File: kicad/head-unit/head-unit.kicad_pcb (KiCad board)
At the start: 4 copper layers, 82 parts, among them J1 Debug_Port, J10 DAC+, J2 Relay_Main_Power, J3 Steering_Wheel, J4 Power_Port, J5 Remote, J6 Relay_Ign_Detect, J7 XT60-M, J8 I2C_Interface, J9 Pi, K1 Relay_Aux_Power, K2 Relay_Amplifier, Q1 NMOS, Q2 NMOS, SW1 SW_RST, U1 STM32F401RCTx, U2 TPS56339DDC, U3 ADP1108AN-3.3

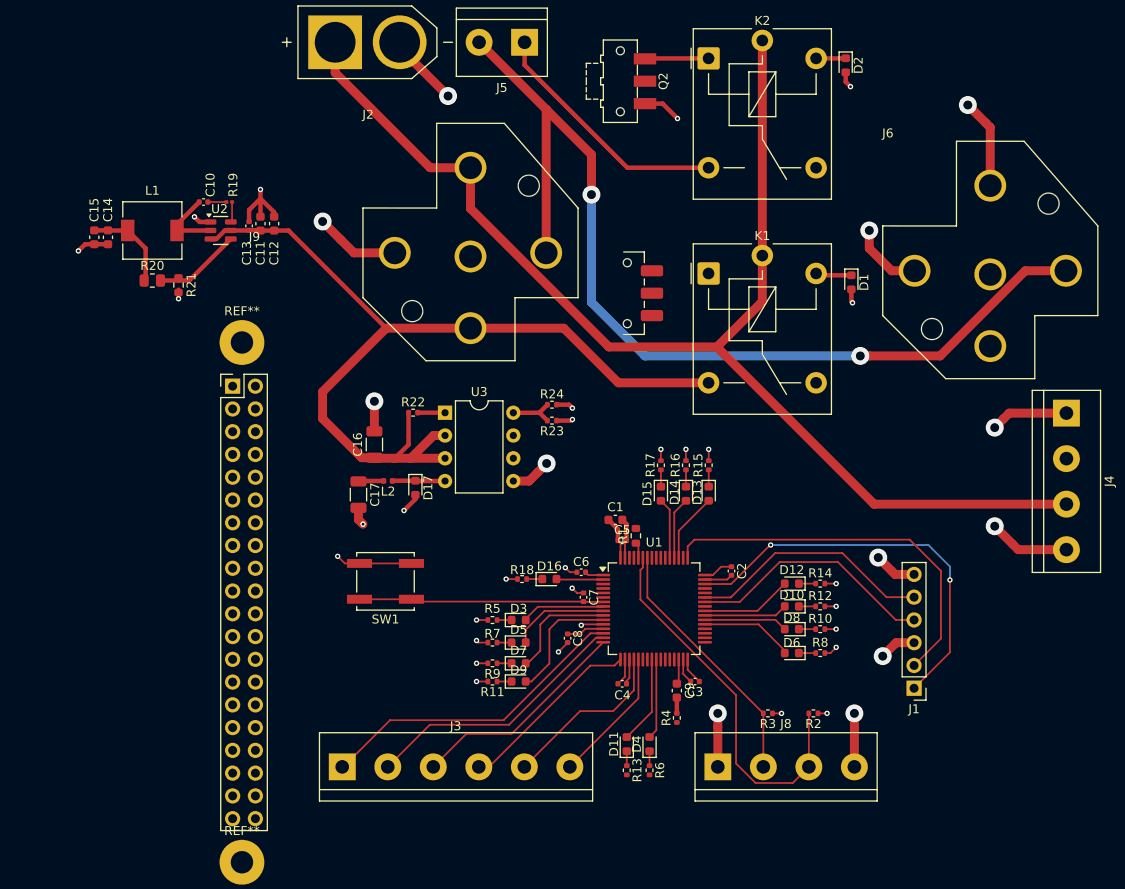
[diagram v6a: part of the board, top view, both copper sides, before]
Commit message: Routing to pi
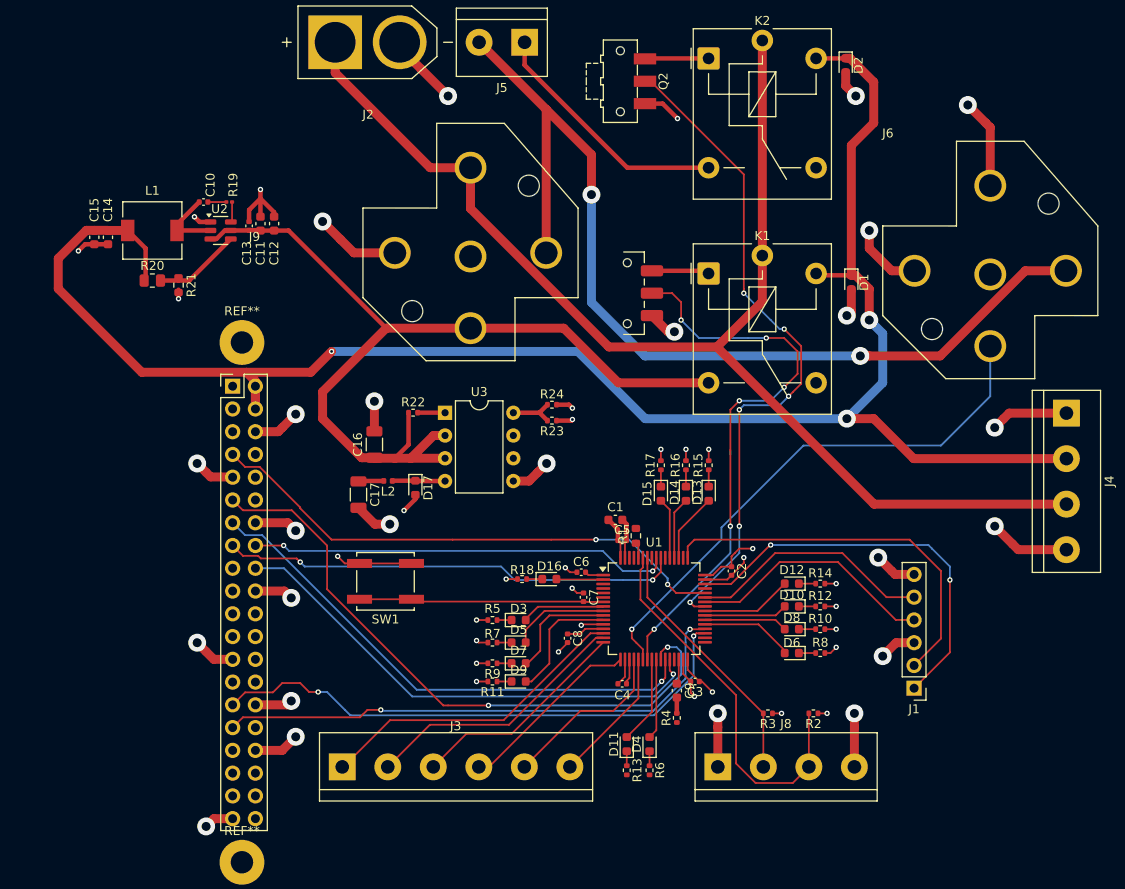
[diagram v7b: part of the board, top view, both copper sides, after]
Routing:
- net +5V: track 17.8 -> 202.0 mm, vias 0 -> 3
- net Amp_Remote_3V3: track 0.00 -> 75.4 mm, vias 0 -> 6
- net AA_Mute: track 0.00 -> 69.9 mm, vias 0 -> 2
- net Aux_Power: track 0.00 -> 64.0 mm, vias 0 -> 6
- net AA_BrightnessUp: track 0.00 -> 61.6 mm, vias 0 -> 2
- net Car_Remote_3V3: track 0.00 -> 61.0 mm, vias 0 -> 1
- net AA_BrightnessDown: track 0.00 -> 60.3 mm, vias 0 -> 2
- net Pi_Ready: track 0.00 -> 59.6 mm, vias 0 -> 2
- net AA_VolUp: track 0.00 -> 58.6 mm, vias 0 -> 1
- net AA_VolDown: track 0.00 -> 55.6 mm, vias 0 -> 1
- net AA_TrackNext: track 0.00 -> 51.3 mm, vias 0 -> 2
- net GND: track 126.0 -> 175.3 mm, vias 34 -> 45
- net AA_TrackPrev: track 0.00 -> 47.2 mm, vias 0 -> 2
- net Net-(Q1-D): track 0.00 -> 6.44 mm
- net +3V3: track 50.9 -> 56.8 mm, vias 8 -> 10

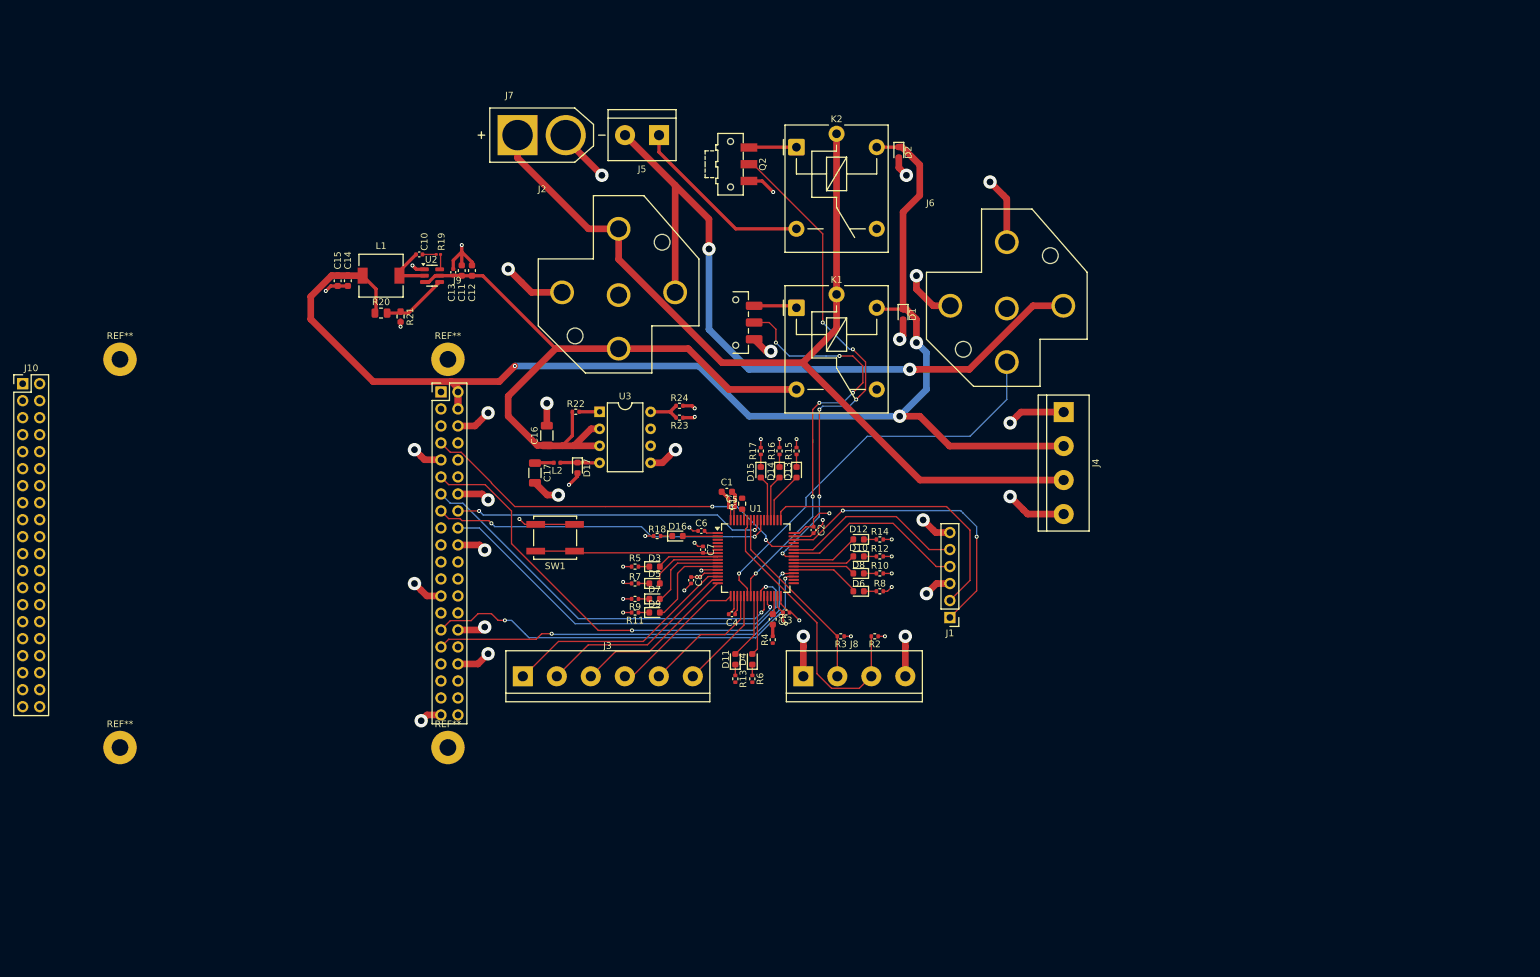
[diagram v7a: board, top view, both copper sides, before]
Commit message: Outline for DAC+; board outline
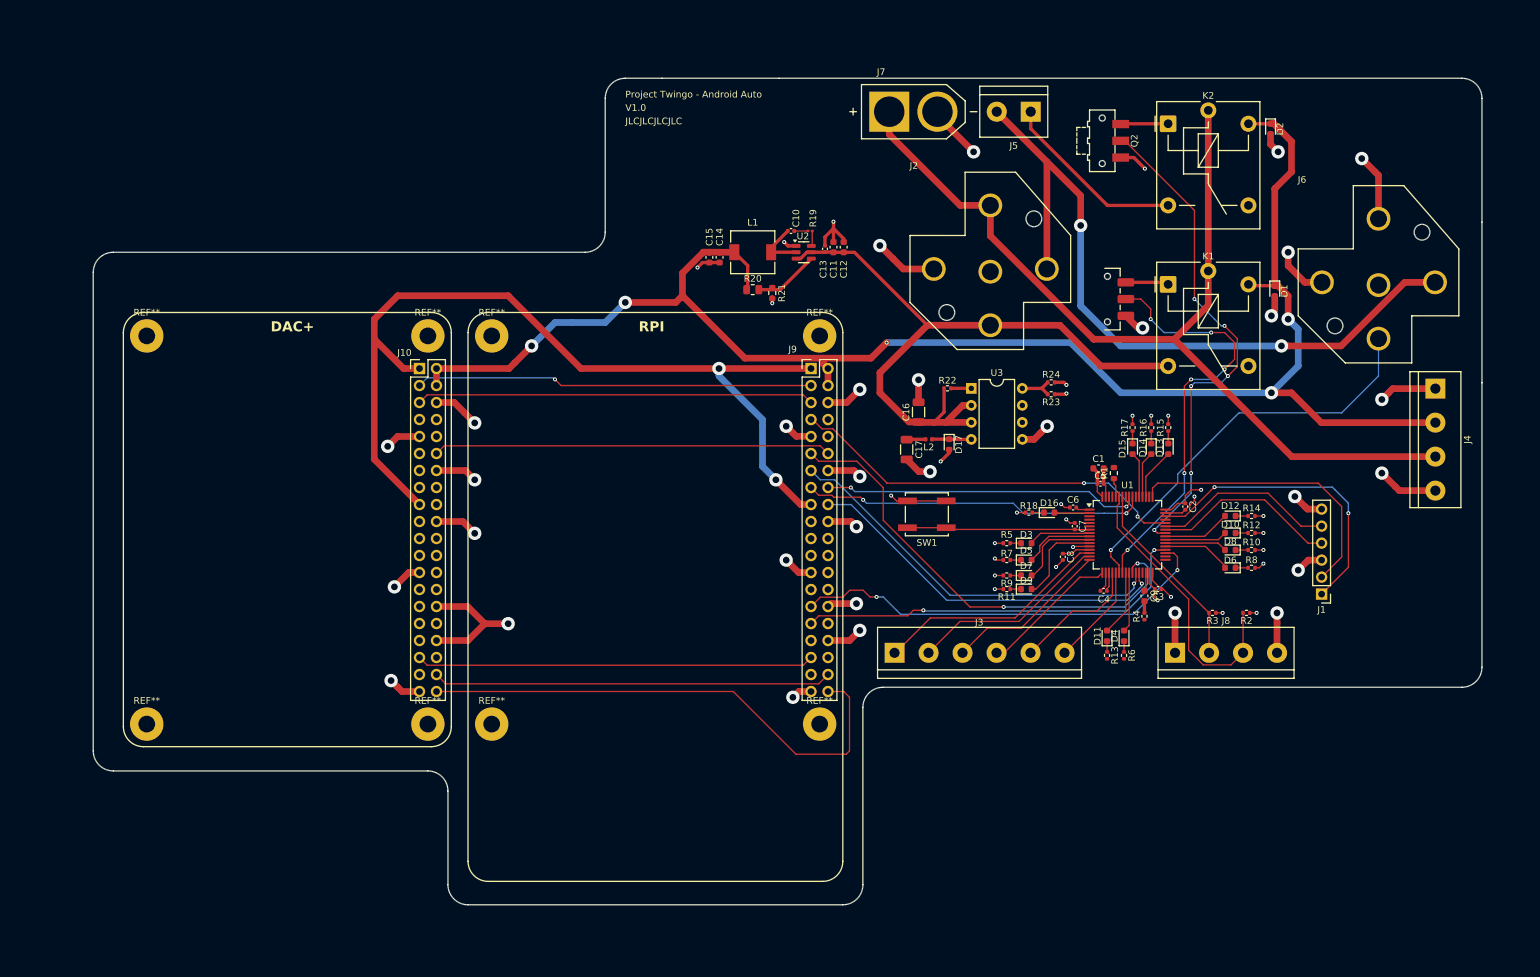
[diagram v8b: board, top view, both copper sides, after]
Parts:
- added REF**: MountingHole_2.5mm_Pad, MountingHole:MountingHole_2.5mm_Pad, F.Cu at (67.0, 117.0)
- added REF**: MountingHole_2.5mm_Pad, MountingHole:MountingHole_2.5mm_Pad, F.Cu at (109.0, 59.0)
- added REF**: MountingHole_2.5mm_Pad, MountingHole:MountingHole_2.5mm_Pad, F.Cu at (109.0, 117.0)
- added REF**: MountingHole_2.5mm_Pad, MountingHole:MountingHole_2.5mm_Pad, F.Cu at (67.0, 59.0)
- moved J10 59.3 mm to (107.8, 63.9)
- moved R1 55.7 mm to (211.5, 79.5)
- moved C1 55.7 mm to (209.2, 78.8)
- moved C4 55.7 mm to (210.0, 97.1)
- moved C9 55.7 mm to (216.1, 97.8)
- moved D10 55.7 mm to (228.9, 88.4)
- moved D12 55.7 mm to (228.9, 85.9)
- moved D2 55.7 mm to (234.9, 28.1)
- moved D4 55.7 mm to (213.0, 103.8)
- moved D6 55.7 mm to (228.9, 93.7)
- moved D8 55.7 mm to (228.9, 91.0)
- moved J4 55.7 mm to (259.5, 66.9)
- moved J5 55.7 mm to (199.1, 25.5)
- moved L2 55.7 mm to (183.8, 74.5)
- moved R3 55.7 mm to (226.2, 100.4)
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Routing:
- net Pi_3V3: track 0.00 -> 137.2 mm, vias 0 -> 2
- net DAC_AUDIO_4: track 0.00 -> 77.4 mm
- net DAC_AUDIO_3: track 0.00 -> 59.7 mm
- net DAC_I2C_SDA: track 0.00 -> 59.5 mm, vias 0 -> 1
- net DAC_AUDIO_1: track 0.00 -> 59.5 mm
- net DAC_I2C_SCL: track 0.00 -> 59.5 mm
- net DAC_AUDIO_2: track 0.00 -> 59.5 mm
- net GND: track 175.3 -> 230.5 mm, vias 45 -> 52
- net +5V: track 202.0 -> 243.2 mm, vias 3 -> 5
- net AA_BrightnessUp: track 61.6 -> 64.0 mm
- net Aux_Power: track 64.0 -> 63.2 mm
- net Net-(U1-BOOT0): track 2.06 -> 2.82 mm
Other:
- board outline added: 207.5 x 123.5 mm
- board text added: "DAC+"
- board text added: "JLCJLCJLCJLC"
- board text added: "Project Twingo - Android Auto"
- board text added: "RPI"
- board text added: "V1.0"
